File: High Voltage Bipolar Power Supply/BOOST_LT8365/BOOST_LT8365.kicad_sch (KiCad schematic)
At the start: 5 parts, among them J3 1715721

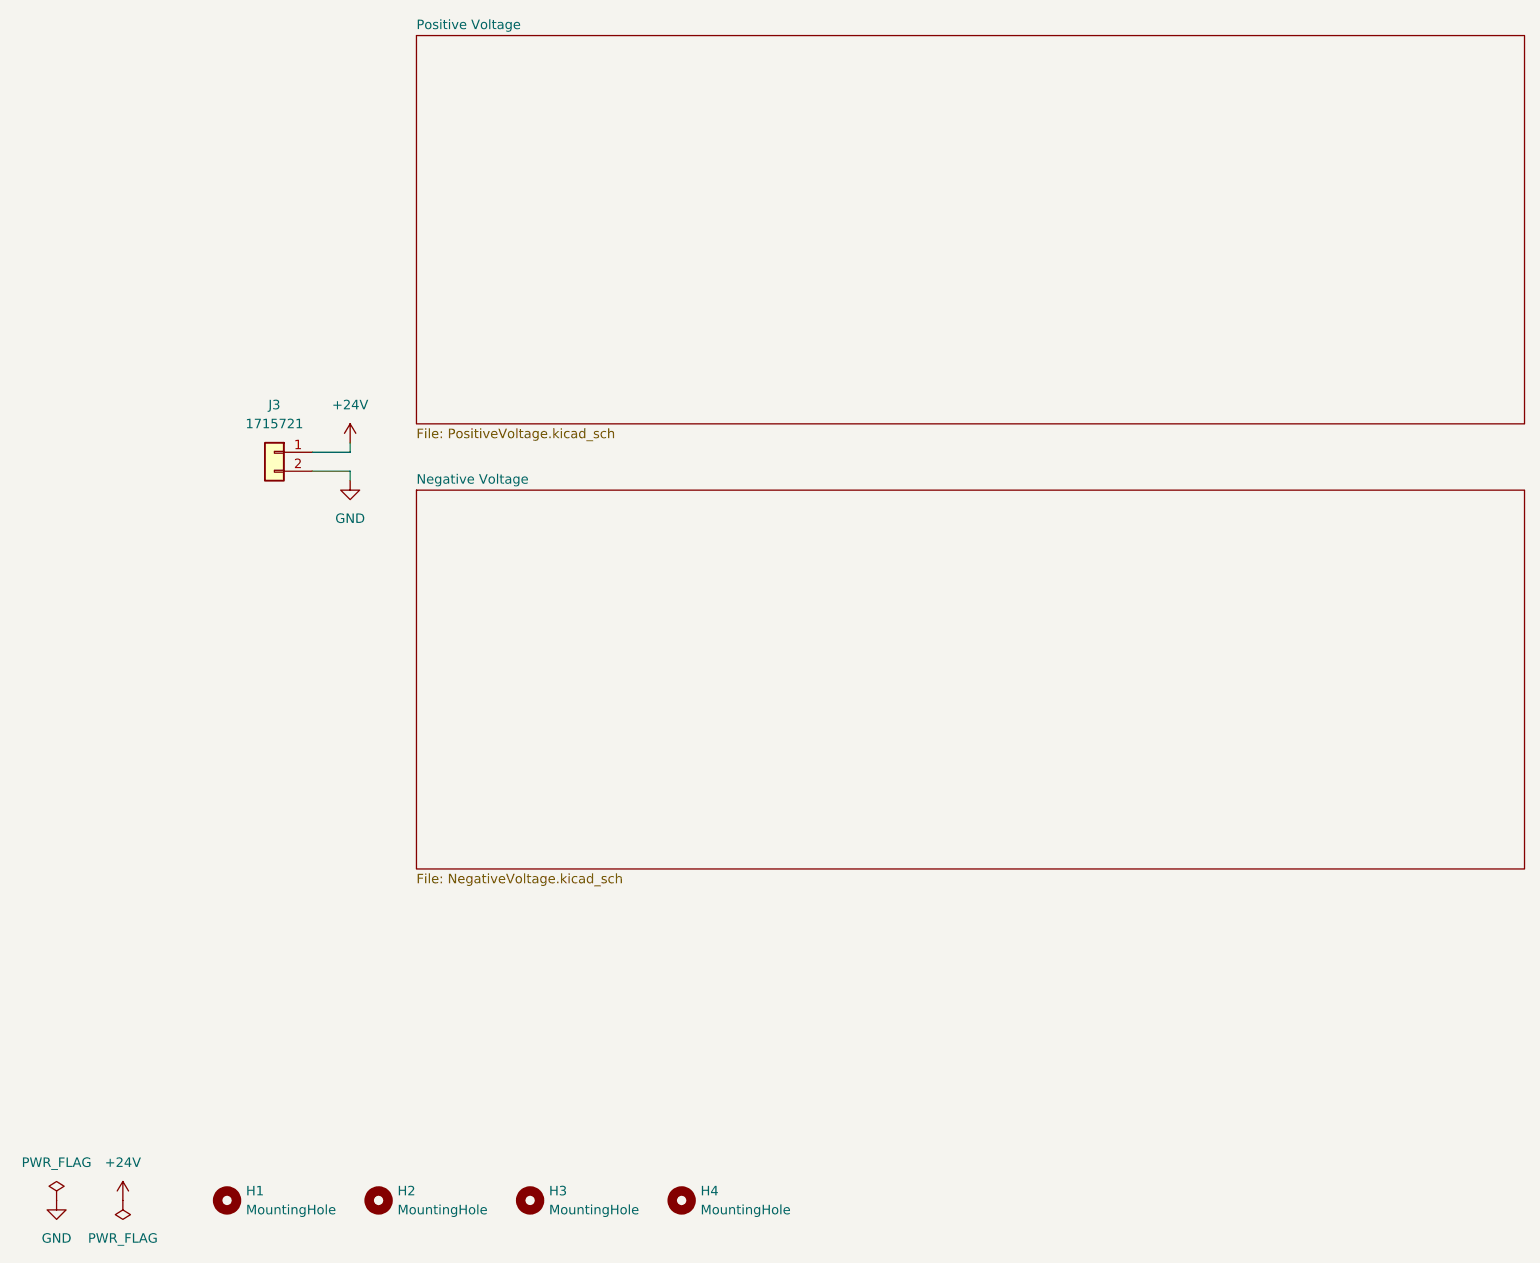
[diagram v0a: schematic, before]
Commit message: BOOST_LT8365 : PCB layout
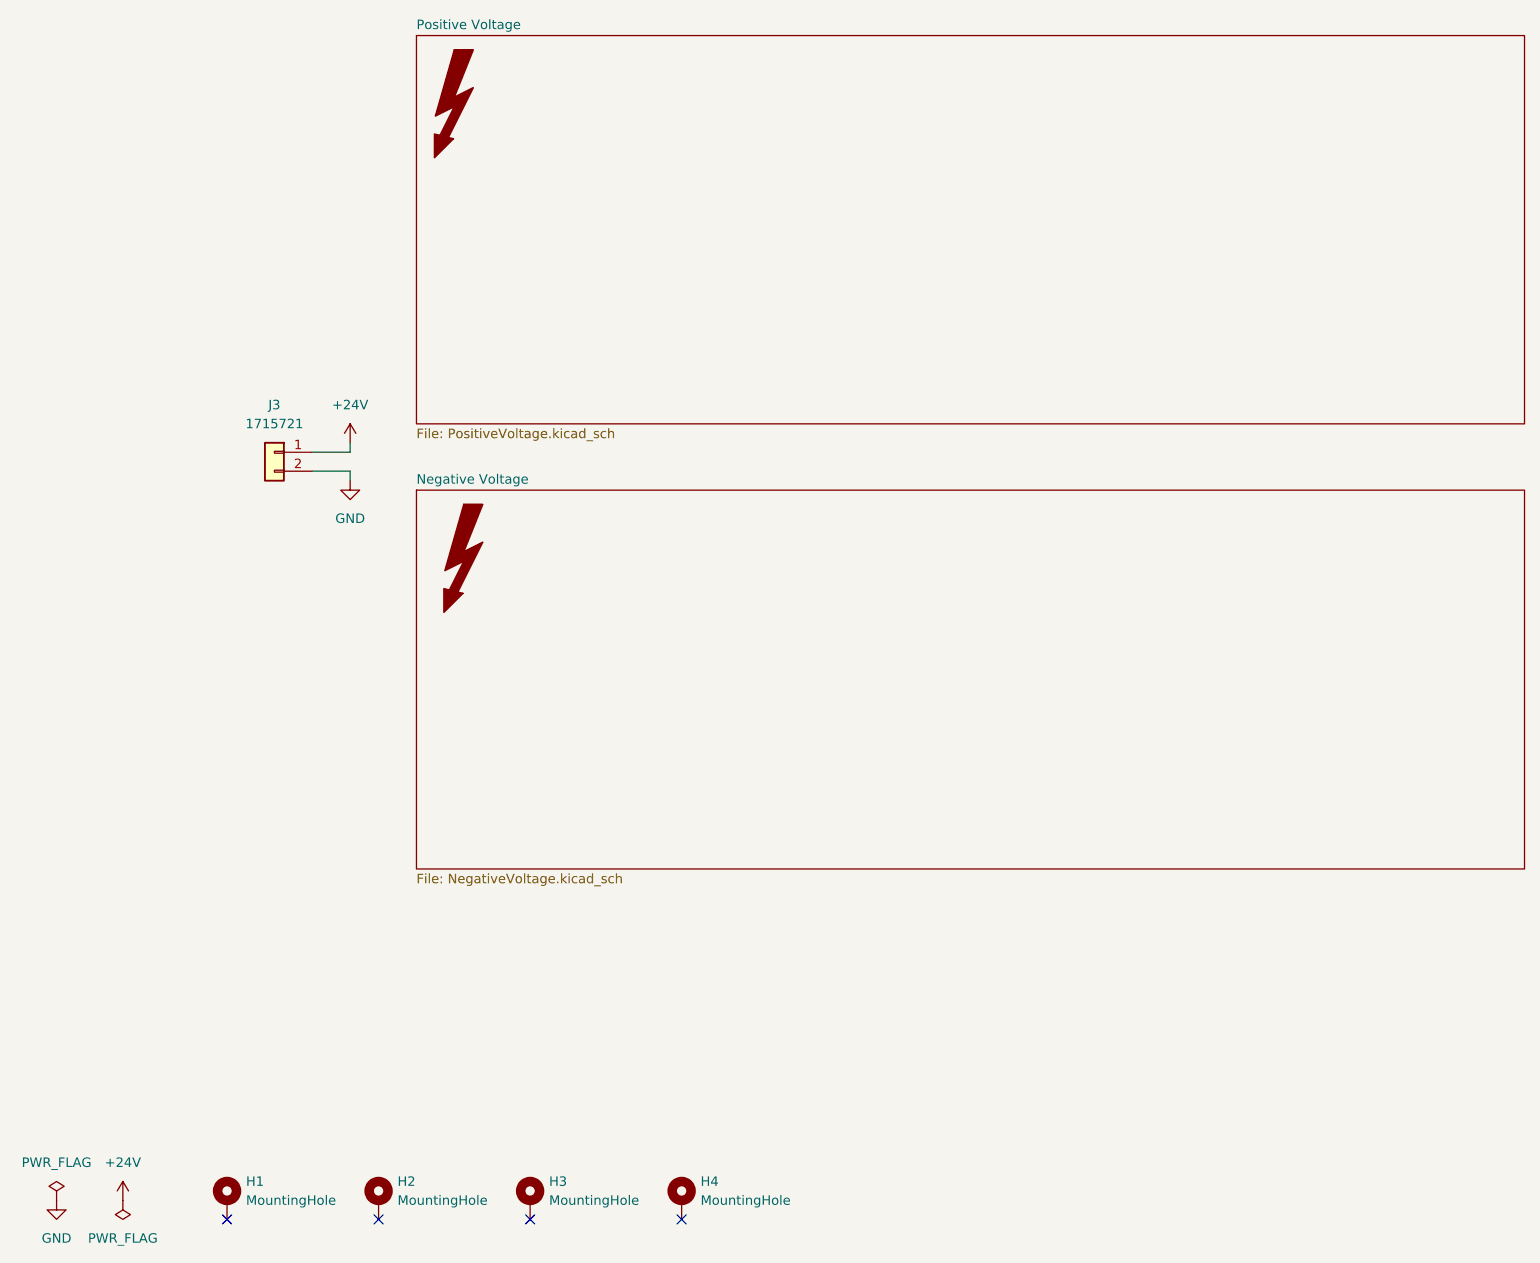
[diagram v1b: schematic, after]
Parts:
- added SYM1, SYM2: SYM_Flash_XLarge, Symbol:Symbol_HighVoltage_Triangle_8x7mm_Copper, symbol Graphic:SYM_Flash_XLarge
- H1, H2, H3, H4: footprint (none) -> MountingHole:MountingHole_3.2mm_M3_DIN965_Pad; symbol Mechanical:MountingHole -> Mechanical:MountingHole_Pad
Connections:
- no-connect marks 0 -> 4
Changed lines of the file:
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@@
 	(generator_version "8.0")
 	(paper "A4")
+	(no_connect
+		(at 48.26 185.42)
+	)
+	(no_connect
+		(at 68.58 185.42)
+	)
+	(no_connect
+		(at 109.22 185.42)
+	)
+	(no_connect
+		(at 88.9 185.42)
+	)
 	(wire
 		(pts
@@
 	)
 	(symbol
+		(lib_id "Graphic:SYM_Flash_XLarge")
+		(at 80.01 97.79 0)
+		(unit 1)
+		(exclude_from_sim no)
+		(in_bom no)
+		(on_board yes)
+		(dnp no)
+		(fields_autoplaced yes)
+		(property "Reference" "SYM1"
+			(at 76.2 97.79 90)
+			(effects
+				(font
+					(size 1.27 1.27)
+				)
+				(hide yes)
+			)
+		)
+		(property "Value" "SYM_Flash_XLarge"
+			(at 83.82 97.79 90)
+			(effects
+				(font
+					(size 1.27 1.27)
+				)
+				(hide yes)
+			)
+		)
+		(property "Footprint" "Symbol:Symbol_HighVoltage_Triangle_8x7mm_Copper"
+			(at 80.01 98.425 0)
+			(effects
+				(font
+					(size 1.27 1.27)
+				)
+				(hide yes)
+			)
+		)
+		(property "Datasheet" "~"
+			(at 90.17 100.33 0)
+			(effects
+				(font
+					(size 1.27 1.27)
+				)
+				(hide yes)
+			)
+		)
+		(property "Description" "Flash symbol, extra large"
+			(at 80.01 97.79 0)
+			(effects
+				(font
+					(size 1.27 1.27)
+				)
+				(hide yes)
+			)
+		)
+		(property "Sim.Enable" "0"
+			(at 80.01 97.79 0)
+			(effects
+				(font
+					(size 1.27 1.27)
+				)
+				(hide yes)
+			)
+		)
+		(instances
+			(project ""
+				(path "/92f9f57b-5733-4cde-b803-f49b57b7d9f1"
+					(reference "SYM1")
+					(unit 1)
+				)
+			)
+		)
+	)
+	(symbol
 		(lib_id "power:GND")
 		(at 25.4 182.88 0)
@@
 	)
 	(symbol
+		(lib_id "Graphic:SYM_Flash_XLarge")
+		(at 78.74 36.83 0)
+		(unit 1)
+		(exclude_from_sim yes)
+		(in_bom no)
+		(on_board yes)
+		(dnp no)
+		(fields_autoplaced yes)
+		(property "Reference" "SYM2"
+			(at 74.93 36.83 90)
+			(effects
+				(font
+					(size 1.27 1.27)
+				)
+				(hide yes)
+			)
+		)
+		(property "Value" "SYM_Flash_XLarge"
+			(at 82.55 36.83 90)
+			(effects
+				(font
+					(size 1.27 1.27)
+				)
+				(hide yes)
+			)
+		)
+		(property "Footprint" "Symbol:Symbol_HighVoltage_Triangle_8x7mm_Copper"
+			(at 78.74 37.465 0)
+			(effects
+				(font
+					(size 1.27 1.27)
+				)
+				(hide yes)
+			)
+		)
+		(property "Datasheet" "~"
+			(at 88.9 39.37 0)
+			(effects
+				(font
+					(size 1.27 1.27)
+				)
+				(hide yes)
+			)
+		)
+		(property "Description" "Flash symbol, extra large"
+			(at 78.74 36.83 0)
+			(effects
+				(font
+					(size 1.27 1.27)
+				)
+				(hide yes)
+			)
+		)
+		(instances
+			(project "BOOST_LT8365"
+				(path "/92f9f57b-5733-4cde-b803-f49b57b7d9f1"
+					(reference "SYM2")
+					(unit 1)
+				)
+			)
+		)
+	)
+	(symbol
 		(lib_id "power:PWR_FLAG")
 		(at 25.4 182.88 0)
@@
 	)
 	(symbol
-		(lib_id "Mechanical:MountingHole")
+		(lib_id "Mechanical:MountingHole_Pad")
 		(at 68.58 182.88 0)
 		(unit 1)
@@
 		(fields_autoplaced yes)
 		(property "Reference" "H2"
-			(at 71.12 181.6099 0)
+			(at 71.12 180.3399 0)
 			(effects
 				(font
@@
 		)
 		(property "Value" "MountingHole"
-			(at 71.12 184.1499 0)
+			(at 71.12 182.8799 0)
 			(effects
 				(font
@@
 			)
 		)
-		(property "Footprint" ""
+		(property "Footprint" "MountingHole:MountingHole_3.2mm_M3_DIN965_Pad"
 			(at 68.58 182.88 0)
 			(effects
@@
 			)
 		)
-		(property "Description" "Mounting Hole without connection"
+		(property "Description" "Mounting Hole with connection"
 			(at 68.58 182.88 0)
 			(effects
@@
 				(hide yes)
 			)
+		)
+		(pin "1"
 		)
 		(instances
@@
 	)
 	(symbol
-		(lib_id "Mechanical:MountingHole")
+		(lib_id "Mechanical:MountingHole_Pad")
 		(at 48.26 182.88 0)
 		(unit 1)
@@
 		(fields_autoplaced yes)
 		(property "Reference" "H1"
-			(at 50.8 181.6099 0)
+			(at 50.8 180.3399 0)
 			(effects
 				(font
@@
 		)
 		(property "Value" "MountingHole"
-			(at 50.8 184.1499 0)
+			(at 50.8 182.8799 0)
 			(effects
 				(font
@@
 			)
 		)
-		(property "Footprint" ""
+		(property "Footprint" "MountingHole:MountingHole_3.2mm_M3_DIN965_Pad"
 			(at 48.26 182.88 0)
 			(effects
@@
 			)
 		)
-		(property "Description" "Mounting Hole without connection"
+		(property "Description" "Mounting Hole with connection"
 			(at 48.26 182.88 0)
 			(effects
@@
 			)
 		)
+		(pin "1"
+		)
 		(instances
 			(project ""
@@
 	)
 	(symbol
-		(lib_id "Mechanical:MountingHole")
+		(lib_id "Mechanical:MountingHole_Pad")
 		(at 109.22 182.88 0)
 		(unit 1)
@@
 		(fields_autoplaced yes)
 		(property "Reference" "H4"
-			(at 111.76 181.6099 0)
+			(at 111.76 180.3399 0)
 			(effects
 				(font
@@
 		)
 		(property "Value" "MountingHole"
-			(at 111.76 184.1499 0)
+			(at 111.76 182.8799 0)
 			(effects
 				(font
@@
 			)
 		)
-		(property "Footprint" ""
+		(property "Footprint" "MountingHole:MountingHole_3.2mm_M3_DIN965_Pad"
 			(at 109.22 182.88 0)
 			(effects
@@
 			)
 		)
-		(property "Description" "Mounting Hole without connection"
+		(property "Description" "Mounting Hole with connection"
 			(at 109.22 182.88 0)
 			(effects
@@
 				(hide yes)
 			)
+		)
+		(pin "1"
 		)
 		(instances
@@
 	)
 	(symbol
-		(lib_id "Mechanical:MountingHole")
+		(lib_id "Mechanical:MountingHole_Pad")
 		(at 88.9 182.88 0)
 		(unit 1)
@@
 		(fields_autoplaced yes)
 		(property "Reference" "H3"
-			(at 91.44 181.6099 0)
+			(at 91.44 180.3399 0)
 			(effects
 				(font
@@
 		)
 		(property "Value" "MountingHole"
-			(at 91.44 184.1499 0)
+			(at 91.44 182.8799 0)
 			(effects
 				(font
@@
 			)
 		)
-		(property "Footprint" ""
+		(property "Footprint" "MountingHole:MountingHole_3.2mm_M3_DIN965_Pad"
 			(at 88.9 182.88 0)
 			(effects
@@
 			)
 		)
-		(property "Description" "Mounting Hole without connection"
+		(property "Description" "Mounting Hole with connection"
 			(at 88.9 182.88 0)
 			(effects
@@
 				(hide yes)
 			)
+		)
+		(pin "1"
 		)
 		(instances
@@
 		)
 		(fill
-			(color 0 0 0 0.0000)
+			(color 255 255 194 1.0000)
 		)
 		(property "Sheetname" "Negative Voltage"
@@
 		)
 		(fill
-			(color 0 0 0 0.0000)
+			(color 255 255 194 1.0000)
 		)
 		(property "Sheetname" "Positive Voltage"

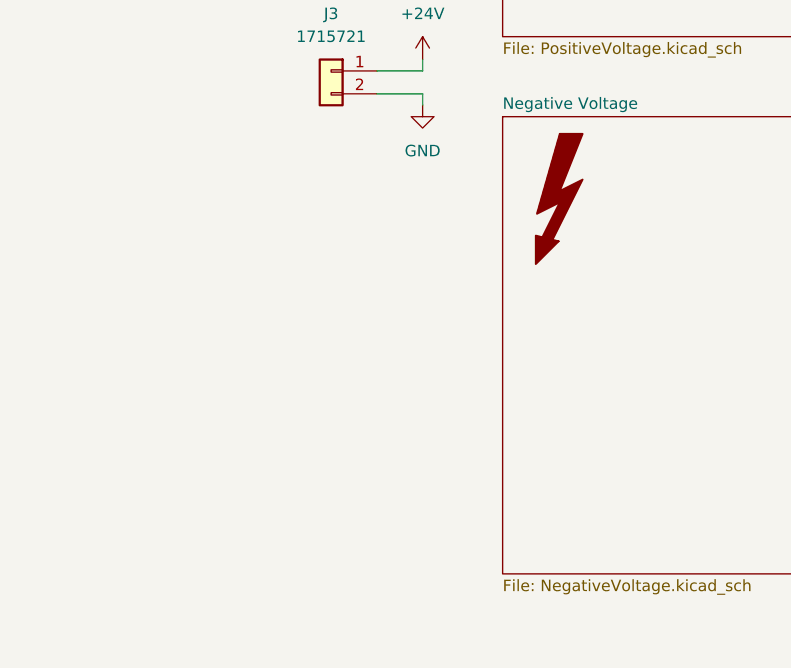
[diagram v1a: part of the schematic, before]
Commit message: BOOST_LT8365 : PCB design done
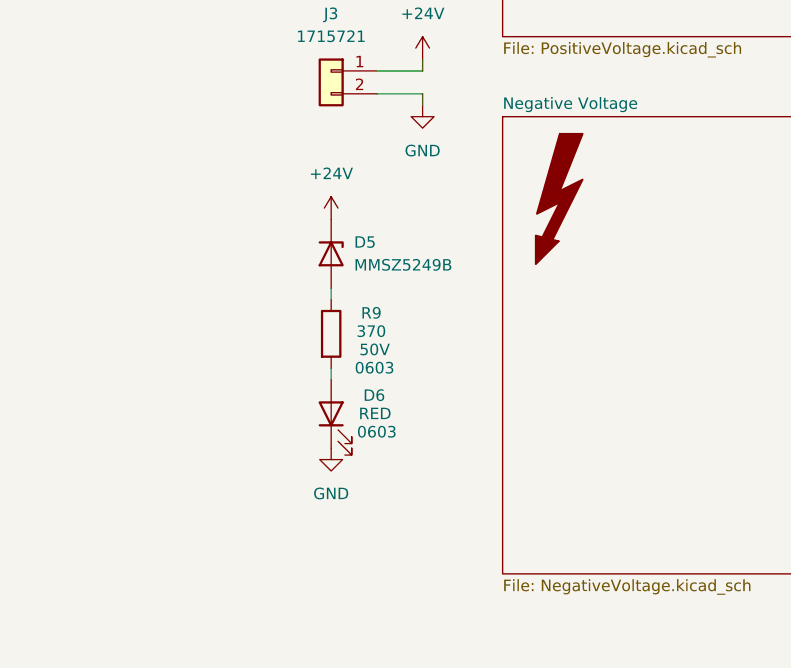
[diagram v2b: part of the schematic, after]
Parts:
- added D5: MMSZ5249B, Diode_SMD:D_SOD-123, symbol Device:D_Zener
- added D6: RED, LED_SMD:LED_0603_1608Metric_Pad1.05x0.95mm_HandSolder, symbol Device:LED
- added R9: 370, Resistor_SMD:R_0603_1608Metric_Pad0.98x0.95mm_HandSolder, symbol Device:R
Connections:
- net +24V: now also D5.1 (K)
- net GND: now also D6.1 (K)
- new net: D5.2 (A), R9.1
- new net: D6.2 (A), R9.2
